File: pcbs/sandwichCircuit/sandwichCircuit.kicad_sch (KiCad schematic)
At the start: 13 parts, among them IC1 3678, J5 Audio Out, U1 ESP32-DevKitC header, U2 CP2104 USB A board

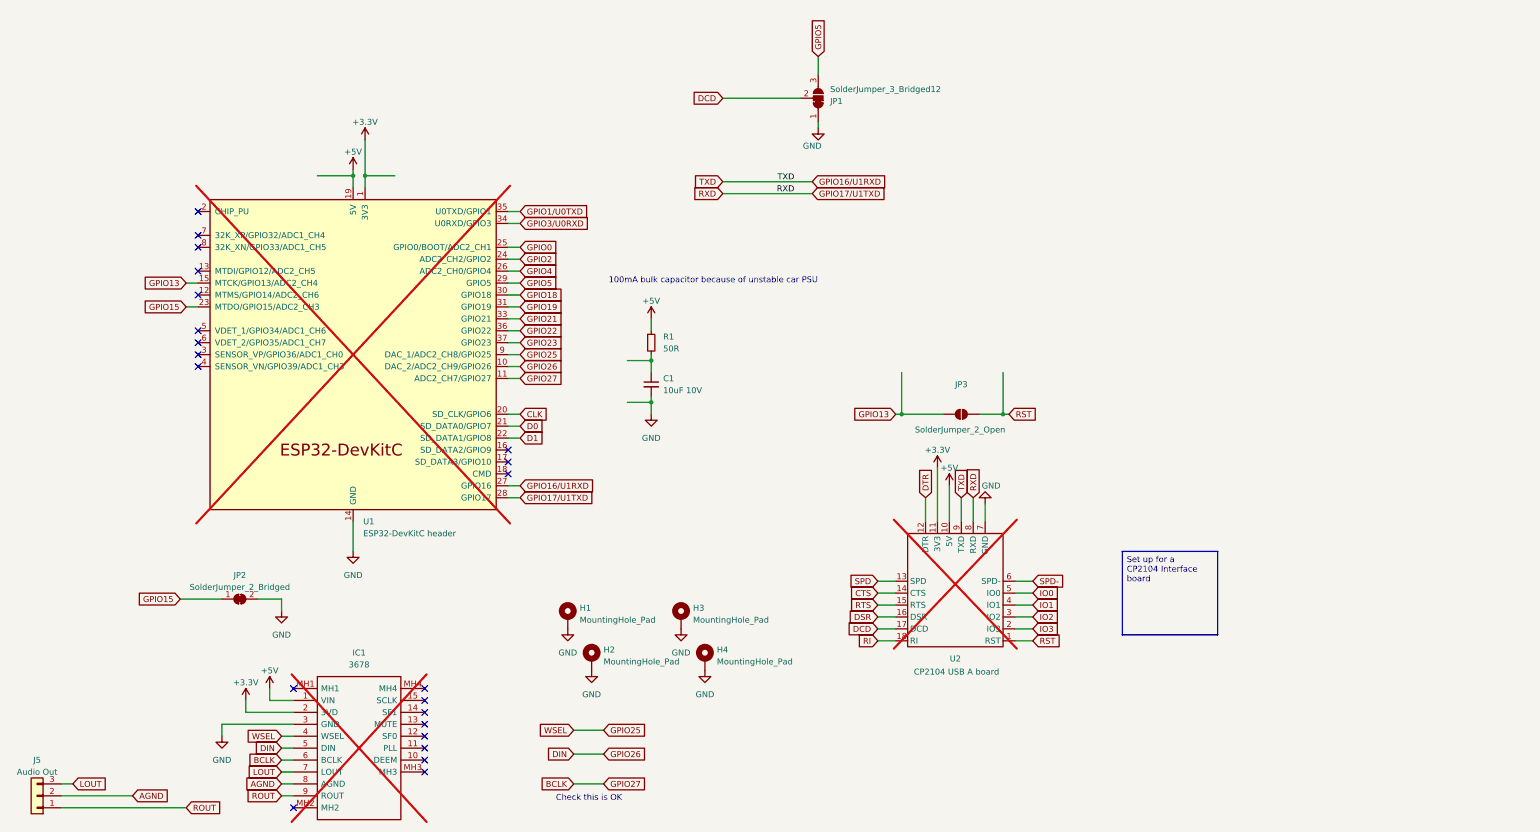
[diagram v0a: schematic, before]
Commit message: SCB aligned to usage of S3
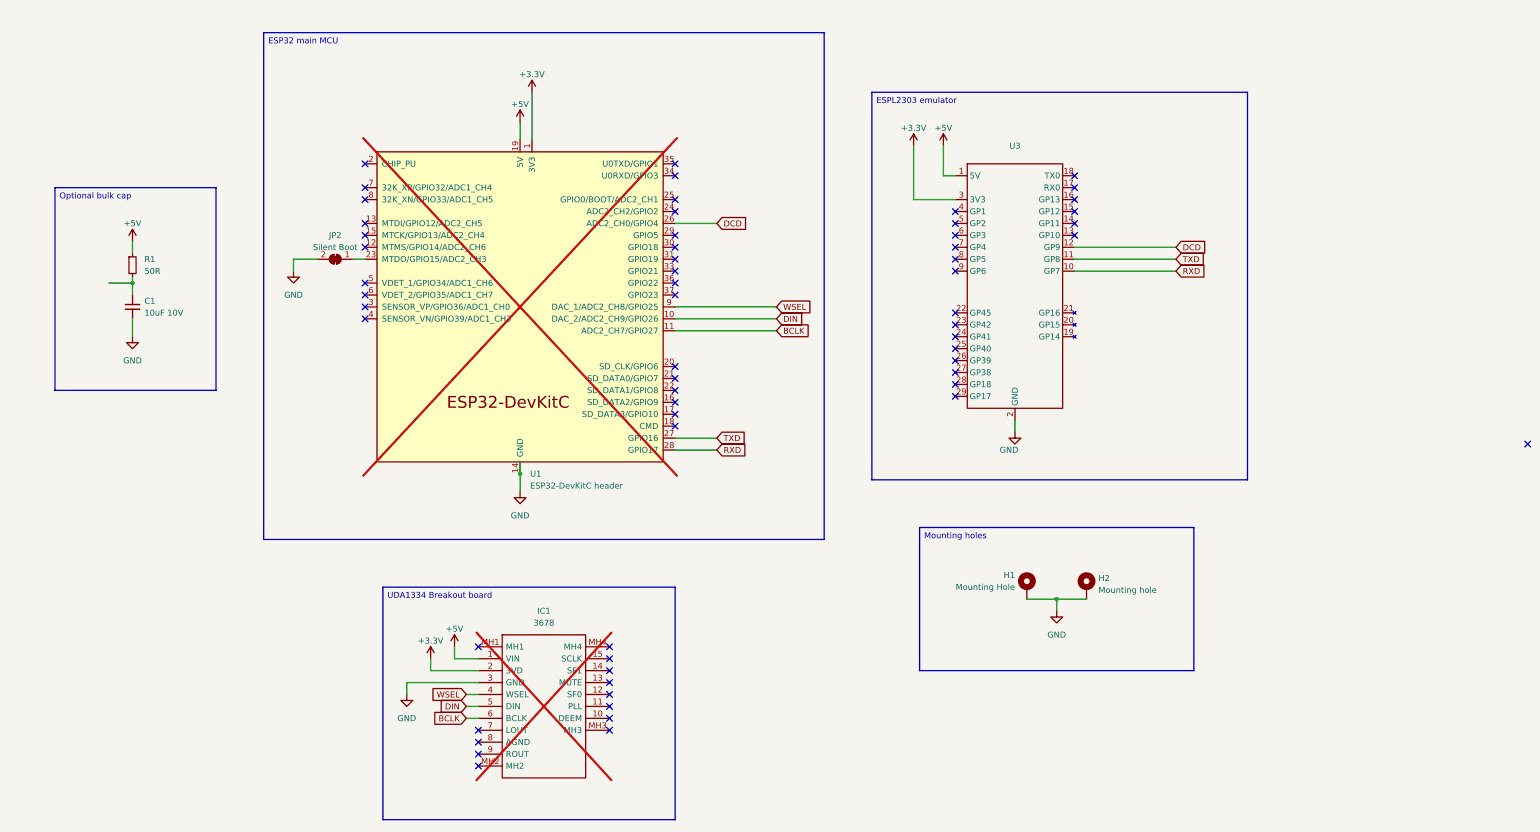
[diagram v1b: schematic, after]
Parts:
- removed H3, H4: MountingHole_Pad, MountingHole:MountingHole_3.2mm_M3_Pad_TopBottom, symbol Mechanical:MountingHole_Pad
- removed J5: Audio Out, Connector_PinHeader_2.54mm:PinHeader_1x03_P2.54mm_Vertical, symbol Connector_Generic:Conn_01x03
- removed JP1: SolderJumper_3_Bridged12, Jumper:SolderJumper-3_P1.3mm_Bridged12_RoundedPad1.0x1.5mm, symbol Jumper:SolderJumper_3_Bridged12
- removed JP3: SolderJumper_2_Open, Jumper:SolderJumper-2_P1.3mm_Open_RoundedPad1.0x1.5mm, symbol Jumper:SolderJumper_2_Open
- removed U2: CP2104 USB A board, DIY:CP2104_USB_Board, symbol DIY:CP2104_UART_Board
- added U3: ~, Project_parts:Waveshare ESP32 S3 Zero THT, symbol ProjectParts:ESP32-S3-Zero
- H1: value MountingHole_Pad -> Mounting Hole
- H2: value MountingHole_Pad -> Mounting hole
- JP2: value SolderJumper_2_Bridged -> Silent Boot; now left out of the parts list
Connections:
- net GPIO4 is gone; now on net DCD: U1.26 (ADC2_CH0/GPIO4)
- net +3.3V: now also U3.3 (3V3)
- net +5V: now also U3.1 (5V)
- net DCD: now also U3.12 (GP9)
- net GND: now also U3.2 (GND)
- net AGND: no longer names the net of IC1.8 (AGND)
- net CLK: no longer names the net of U1.20 (SD_CLK/GPIO6)
- net D0: no longer names the net of U1.21 (SD_DATA0/GPIO7)
- net D1: no longer names the net of U1.22 (SD_DATA1/GPIO8)
- net GPIO0: no longer names the net of U1.25 (GPIO0/BOOT/ADC2_CH1)
- net GPIO13: no longer names the net of U1.15 (MTCK/GPIO13/ADC2_CH4)
- net GPIO15: no longer names the net of JP2.1 (A), U1.23 (MTDO/GPIO15/ADC2_CH3)
- net GPIO16/U1RXD renamed TXD
- net TXD: now also U3.11 (GP8)
- net GPIO17/U1TXD renamed RXD
- net RXD: now also U3.10 (GP7)
- net GPIO18: no longer names the net of U1.30 (GPIO18)
- net GPIO19: no longer names the net of U1.31 (GPIO19)
- net GPIO1/U0TXD: no longer names the net of U1.35 (U0TXD/GPIO1)
- net GPIO2: no longer names the net of U1.24 (ADC2_CH2/GPIO2)
- net GPIO21: no longer names the net of U1.33 (GPIO21)
- net GPIO22: no longer names the net of U1.36 (GPIO22)
- net GPIO23: no longer names the net of U1.37 (GPIO23)
- net GPIO25 renamed WSEL
- net GPIO3/U0RXD: no longer names the net of U1.34 (U0RXD/GPIO3)
- net GPIO5: no longer names the net of U1.29 (GPIO5)
- net LOUT: no longer names the net of IC1.7 (LOUT)
- net ROUT: no longer names the net of IC1.9 (ROUT)
- no-connect marks 22 -> 60
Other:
- note removed: "100mA bulk capacitor because of unstable car PSU"
- note removed: "Check this is OK"
- title: Simple carrier board (CP2104) -> Simple carrier board
- moved on the sheet: C1, H1, H2, IC1, JP2, R1, U1
